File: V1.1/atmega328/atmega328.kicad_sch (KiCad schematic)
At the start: 17 parts

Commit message: things
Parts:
- removed C2, C8, C9: (no value), symbol Device:C_Small
- removed D1: (no value), symbol Device:LED
- removed L1: (no value), symbol Device:L
- removed R6: (no value), symbol Device:R
- removed U2: (no value), symbol Regulator_Switching:TPS62203DBV
- added C2: 4.7, Capacitor_Tantalum_SMD:CP_EIA-3216-18_Kemet-A, symbol Device:C_Polarized_Small
- added C5, C?: 100n, Capacitor_SMD:C_0402_1005Metric, symbol Device:C_Small
- added C6: 20p, Capacitor_SMD:C_0402_1005Metric, symbol Device:C_Small
- added D1: BZV55C6V2, Diode_SMD:D_MiniMELF, symbol Diode:BZV55B10
- added D2: RED_LED, LED_SMD:LED_0603_1608Metric, symbol Device:LED_Small
- added J1: Conn_01x08_Female, Connector_PinSocket_2.54mm:PinSocket_1x08_P2.54mm_Vertical, symbol Connector:Conn_01x08_Female
- added J3: Conn_01x02_Male, Connector_PinHeader_2.54mm:PinHeader_1x02_P2.54mm_Vertical, symbol Connector:Conn_01x02_Male
- added J?: Conn_01x04_Female, Connector_PinSocket_2.54mm:PinSocket_1x04_P2.54mm_Vertical, symbol Connector:Conn_01x04_Female
- added JP1: SolderJumper_2_Open, Jumper:SolderJumper-2_P1.3mm_Open_Pad1.0x1.5mm, symbol Jumper:SolderJumper_2_Open
- added JP? (x3): SolderJumper_3_Open, Jumper:SolderJumper-3_P1.3mm_Open_RoundedPad1.0x1.5mm_NumberLabels, symbol Jumper:SolderJumper_3_Open
- added Q1: Si2319CDS, Package_TO_SOT_SMD:SOT-23, symbol Transistor_FET:Si2319CDS
- added R2: 10k, Resistor_SMD:R_0603_1608Metric, symbol Device:R_Small
- added R3: 20k, Resistor_SMD:R_0603_1608Metric, symbol Device:R_Small
- +5V1: renamed from 3.3v1; value (none) -> Conn_01x01; footprint (none) -> Connector_PinHeader_2.54mm:PinHeader_1x01_P2.54mm_Vertical
- C1: value (none) -> 100n; footprint (none) -> Capacitor_SMD:C_0603_1608Metric; LCSC (none) -> C346191
- C3, C4: value (none) -> 100n; footprint (none) -> Capacitor_SMD:C_0402_1005Metric; LCSC (none) -> C1525
- C7: value (none) -> 20p; footprint (none) -> Capacitor_SMD:C_0402_1005Metric; LCSC (none) -> C880615
- ISP1: value (none) -> Conn_02x03_Top_Bottom; footprint (none) -> Connector_PinSocket_2.54mm:isp_6pin
- R1: value (none) -> 100k; footprint (none) -> Resistor_SMD:R_0603_1608Metric; LCSC (none) -> C14675
- U1: value (none) -> ATmega328P-AU; footprint (none) -> Package_QFP:TQFP-32_7x7mm_P0.8mm
- Y1: value (none) -> Crystal; footprint (none) -> Crystal:Crystal_SMD_5032-2Pin_5.0x3.2mm; LCSC (none) -> C122521
- gave numbers to parts that had none: 1
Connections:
- net GND: now also R1.2, U3.13 (GND), C2.2, C5.2, C6.2, C?.2, J1.7 (Pin_7), J?.1 (Pin_1), JP1.1 (A), R3.1
- net LED_PWR: no longer R1.1
- net MISO: now also U3.3 (MISO)
- net MOSI: now also U3.4 (MOSI)
- net RESET: now also R2.1
- net RX: now also J?.3 (Pin_3)
- net SCK: now also U3.2 (CLK)
- net TX: now also J?.2 (Pin_2)
- net XTAL1: now also C6.1; no longer C3.1
- net XTAL2: now also C7.1; no longer C4.1
- net Wuc: now reaches U1.25 (PC2)
- net Wuc: now also JP?.3 (B)
- net CS: now reaches U3.1 (~{CS})
- net Uas: now reaches U3.10 (U)
- net Uas: now also JP?.1 (A)
- net +5V: now reaches U3.11 (VDD)
- net +5V: now also +5V1.1 (Pin_1), C3.1, C4.1, U1.6 (VCC), C5.1, C?.1, D1.1 (K), D2.2 (A), J?.4 (Pin_4), Q1.2 (S), R2.2
- net Was: now reaches U3.8 (W/PWM)
- net Was: now also JP?.1 (A)
- net Vas: now reaches U3.9 (V)
- net Vas: now also JP?.1 (A)
- removed net +3V3: +5V1.1 (Pin_1), C7.1, ISP1.2 (Pin_2), U1.18 (AVCC), U1.4 (VCC), U1.6 (VCC)
- net LED1 renamed Uuc
- net Uuc: now also JP?.3 (B)
- net LED2 renamed Vuc
- net Vuc: now also JP?.3 (B)
- net VCC renamed Vcc
- net Vcc: now also C2.1, J1.1 (Pin_1), J1.8 (Pin_8), Q1.3 (D)
- new net: D1.2 (A), Q1.1 (G), R1.1
- new net: D2.1 (K), R3.2
- new net 3.3V: ISP1.2 (Pin_2)
- new net DCAP2: U1.4 (VCC)
- new net DCAP3: U1.18 (AVCC)
- new net TRM1: J1.5 (Pin_5), J3.1 (Pin_1)
- new net TRM2: J1.6 (Pin_6), J3.2 (Pin_2), JP1.2 (B)
- new net U: J1.2 (Pin_2), JP?.2 (C)
- new net V: J1.3 (Pin_3), JP?.2 (C)
- new net W: J1.4 (Pin_4), JP?.2 (C)
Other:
- note added: "motor thermistor two wires lead from motor to PCB"
- note added: "reverse polarity protection"
- moved on the sheet: +5V1, ISP1, U1, U3, Y1

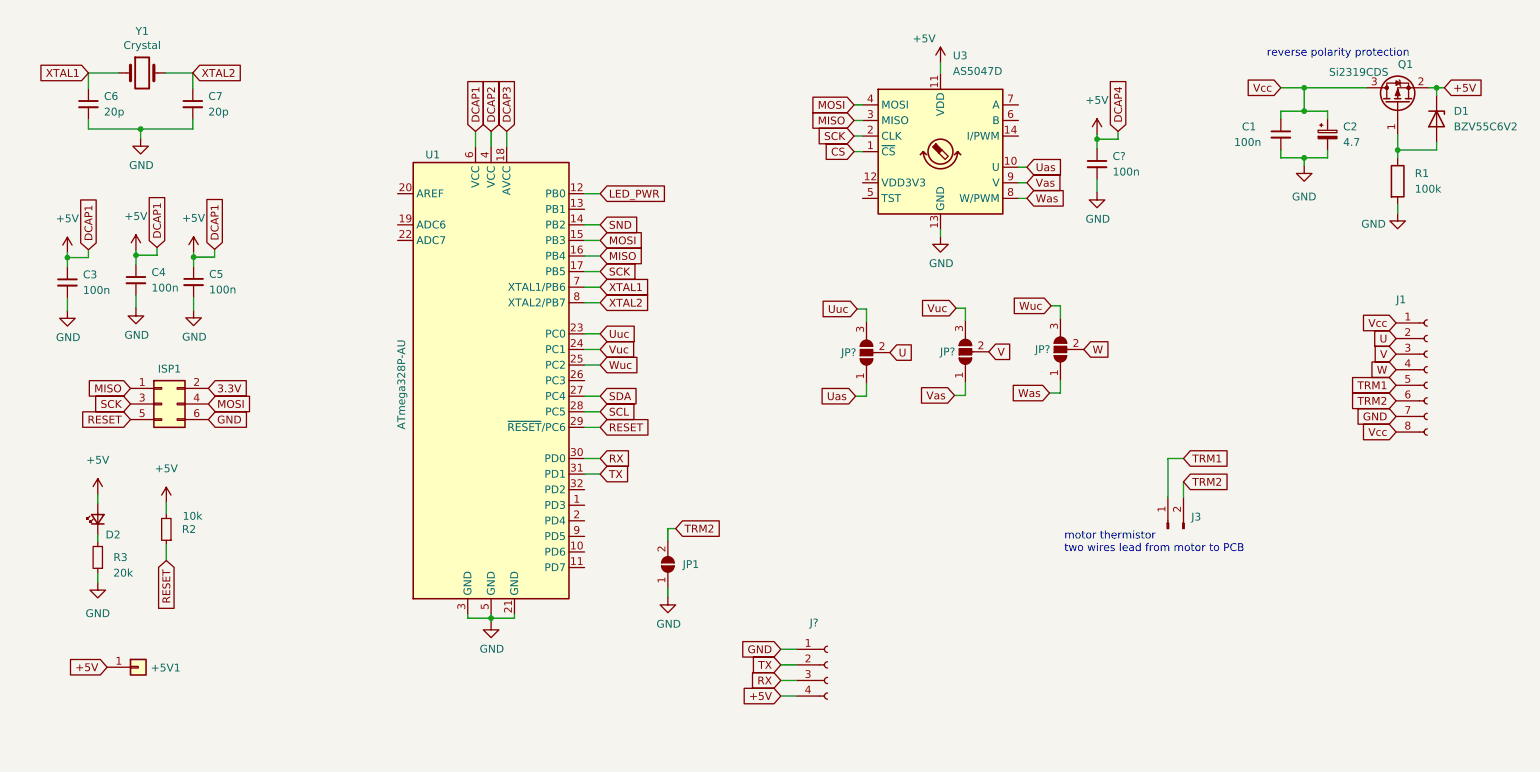
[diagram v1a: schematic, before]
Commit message: recreating lost AS5048 version
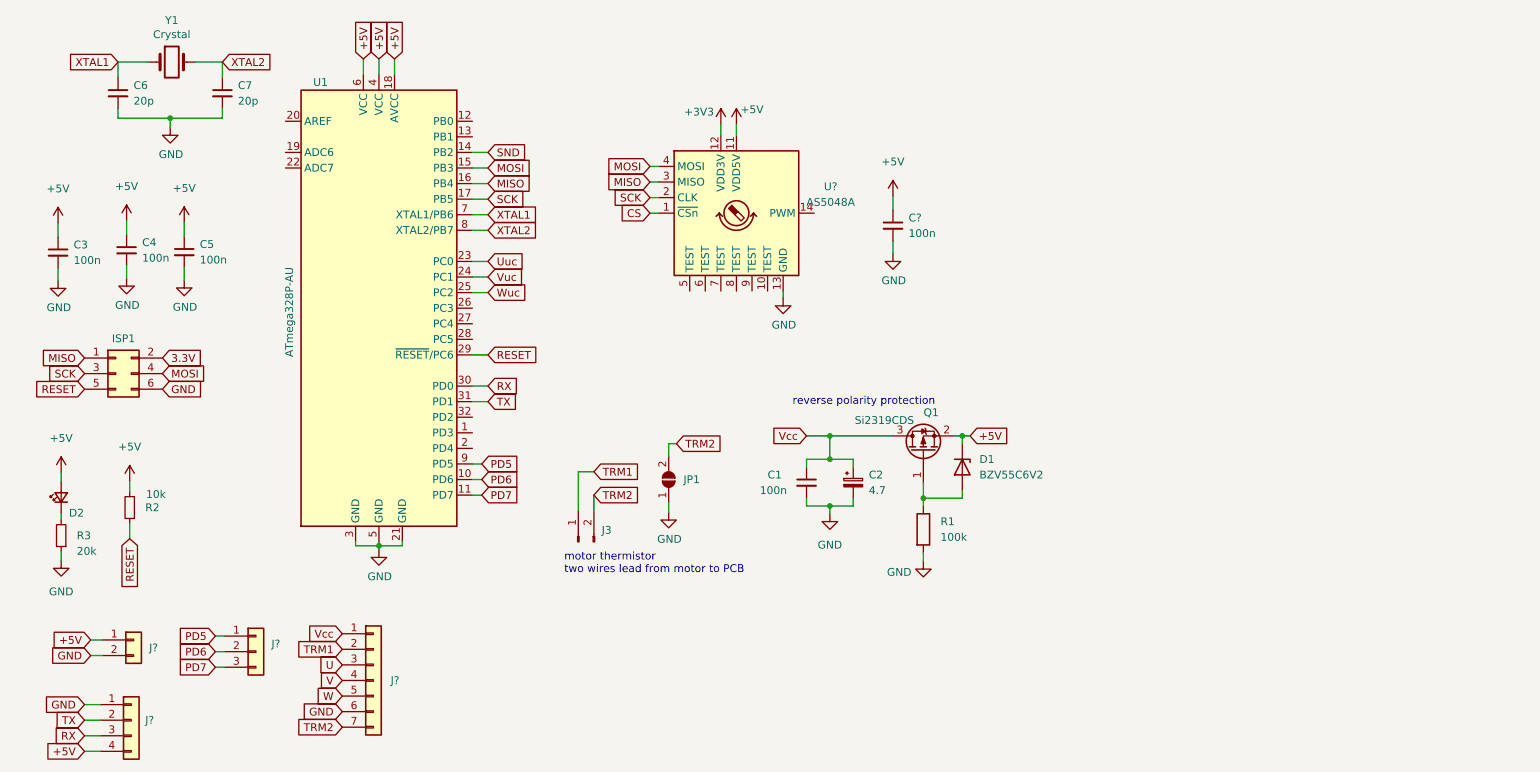
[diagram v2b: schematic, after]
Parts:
- removed +5V1: Conn_01x01, Connector_PinHeader_2.54mm:PinHeader_1x01_P2.54mm_Vertical, symbol Connector_Generic:Conn_01x01
- removed J1: Conn_01x08_Female, Connector_PinSocket_2.54mm:PinSocket_1x08_P2.54mm_Vertical, symbol Connector:Conn_01x08_Female
- removed J?: Conn_01x04_Female, Connector_PinSocket_2.54mm:PinSocket_1x04_P2.54mm_Vertical, symbol Connector:Conn_01x04_Female
- removed JP? (x3): SolderJumper_3_Open, Jumper:SolderJumper-3_P1.3mm_Open_RoundedPad1.0x1.5mm_NumberLabels, symbol Jumper:SolderJumper_3_Open
- removed U3: AS5047D, Package_SO:TSSOP-14_4.4x5mm_P0.65mm, symbol Sensor_Magnetic:AS5047D
- added J?: Conn_01x04, symbol Connector_Generic:Conn_01x04
- added J?: Conn_01x03, symbol Connector_Generic:Conn_01x03
- added J?: Conn_01x07, symbol Connector_Generic:Conn_01x07
- added J?: Conn_01x02, symbol Connector_Generic:Conn_01x02
- added U?: AS5048A, Package_SO:TSSOP-14_4.4x5mm_P0.65mm, symbol Sensor_Magnetic:AS5048A
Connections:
- net DCAP2 is gone; now on net +5V: U1.4 (VCC)
- net DCAP3 is gone; now on net +5V: U1.18 (AVCC)
- net +5V: now also J?.1 (Pin_1), J?.4 (Pin_4), U?.11 (VDD5V)
- net CS: now also U?.1 (~{CSn})
- net GND: now also J?.1 (Pin_1), J?.2 (Pin_2), J?.6 (Pin_6), U?.13 (GND)
- net MISO: now also U?.3 (MISO)
- net MOSI: now also U?.4 (MOSI)
- net RX: now also J?.3 (Pin_3)
- net SCK: now also U?.2 (CLK)
- net TRM1: now also J?.2 (Pin_2)
- net TRM2: now also J?.7 (Pin_7)
- net TX: now also J?.2 (Pin_2)
- net U: now also J?.3 (Pin_3)
- net V: now also J?.4 (Pin_4)
- net Vcc: now also J?.1 (Pin_1)
- net W: now also J?.5 (Pin_5)
- net PD6: now reaches U1.10 (PD6)
- net PD6: now also J?.2 (Pin_2)
- net PD7: now reaches U1.11 (PD7)
- net PD7: now also J?.3 (Pin_3)
- net PD5: now reaches U1.9 (PD5)
- net PD5: now also J?.1 (Pin_1)
- net LED_PWR: no longer names the net of U1.12 (PB0)
- net SCL: no longer names the net of U1.28 (PC5)
- net SDA: no longer names the net of U1.27 (PC4)
- new net +3V3: U?.12 (VDD3V)
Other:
- moved on the sheet: C1, C2, C3, C4, C5, C6, C7, C?, D1, D2, ISP1, J3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

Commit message: recreating lost AS5048 version
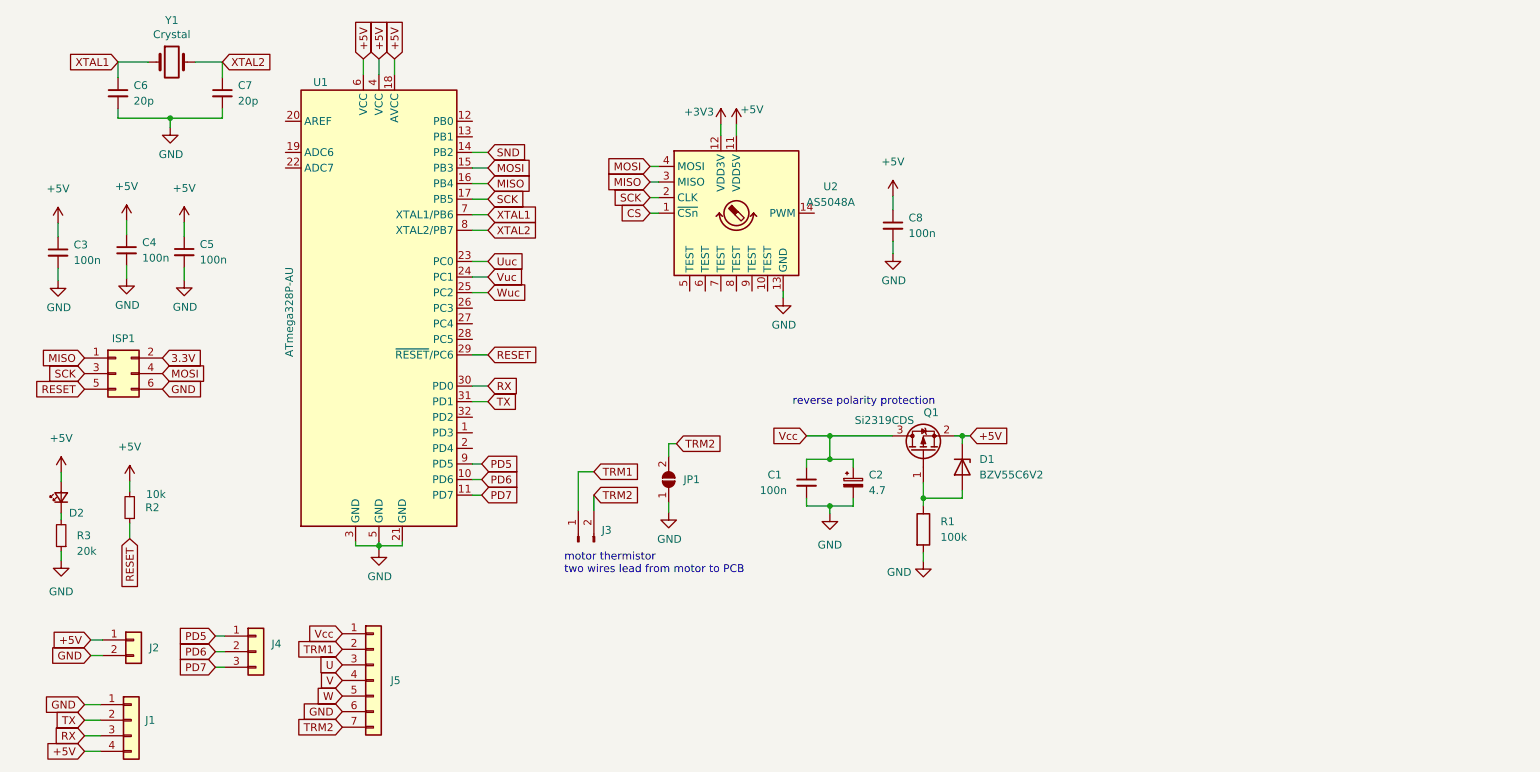
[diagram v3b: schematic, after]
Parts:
- gave numbers to parts that had none: 6
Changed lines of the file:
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@@
   (symbol (lib_id "Connector_Generic:Conn_01x04") (at 34.544 129.794 0) (unit 1)
     (in_bom yes) (on_board yes) (fields_autoplaced)
-    (property "Reference" "J?" (id 0) (at 36.83 129.7939 0)
+    (property "Reference" "J1" (id 0) (at 36.83 129.7939 0)
       (effects (font (size 1.27 1.27)) (justify left))
     )
@@
   (symbol (lib_id "Device:C_Small") (at 158.75 49.149 0) (unit 1)
     (in_bom yes) (on_board yes)
-    (property "Reference" "C?" (id 0) (at 161.29 47.879 0)
+    (property "Reference" "C8" (id 0) (at 161.29 47.879 0)
       (effects (font (size 1.27 1.27)) (justify left))
     )
@@
   (symbol (lib_id "power:GND") (at 140.843 60.96 0) (unit 1)
     (in_bom yes) (on_board yes)
-    (property "Reference" "#PWR?" (id 0) (at 140.843 67.31 0)
+    (property "Reference" "#PWR0102" (id 0) (at 140.843 67.31 0)
       (effects (font (size 1.27 1.27)) hide)
     )
@@
   (symbol (lib_id "power:+3V3") (at 130.683 32.639 0) (unit 1)
     (in_bom yes) (on_board yes)
-    (property "Reference" "#PWR?" (id 0) (at 130.683 36.449 0)
+    (property "Reference" "#PWR0107" (id 0) (at 130.683 36.449 0)
       (effects (font (size 1.27 1.27)) hide)
     )
@@
   (symbol (lib_id "Connector_Generic:Conn_01x03") (at 54.864 118.618 0) (unit 1)
     (in_bom yes) (on_board yes)
-    (property "Reference" "J?" (id 0) (at 57.404 117.3479 0)
+    (property "Reference" "J4" (id 0) (at 57.404 117.3479 0)
       (effects (font (size 1.27 1.27)) (justify left))
     )
@@
   (symbol (lib_id "power:GND") (at 158.75 53.721 0) (unit 1)
     (in_bom yes) (on_board yes)
-    (property "Reference" "#PWR?" (id 0) (at 158.75 60.071 0)
+    (property "Reference" "#PWR0103" (id 0) (at 158.75 60.071 0)
       (effects (font (size 1.27 1.27)) hide)
     )
@@
   (symbol (lib_id "Connector_Generic:Conn_01x07") (at 74.041 123.317 0) (unit 1)
     (in_bom yes) (on_board yes) (fields_autoplaced)
-    (property "Reference" "J?" (id 0) (at 76.835 123.3169 0)
+    (property "Reference" "J5" (id 0) (at 76.835 123.3169 0)
       (effects (font (size 1.27 1.27)) (justify left))
     )
@@
   (symbol (lib_id "power:+5V") (at 158.75 44.323 0) (unit 1)
     (in_bom yes) (on_board yes) (fields_autoplaced)
-    (property "Reference" "#PWR?" (id 0) (at 158.75 48.133 0)
+    (property "Reference" "#PWR0104" (id 0) (at 158.75 48.133 0)
       (effects (font (size 1.27 1.27)) hide)
     )
@@
   (symbol (lib_id "Connector_Generic:Conn_01x02") (at 34.925 116.713 0) (unit 1)
     (in_bom yes) (on_board yes) (fields_autoplaced)
-    (property "Reference" "J?" (id 0) (at 37.465 117.9829 0)
+    (property "Reference" "J2" (id 0) (at 37.465 117.9829 0)
       (effects (font (size 1.27 1.27)) (justify left))
     )
@@
   (symbol (lib_id "power:GND") (at 122.174 95.885 0) (unit 1)
     (in_bom yes) (on_board yes)
-    (property "Reference" "#PWR?" (id 0) (at 122.174 102.235 0)
+    (property "Reference" "#PWR0101" (id 0) (at 122.174 102.235 0)
       (effects (font (size 1.27 1.27)) hide)
     )
@@
   (symbol (lib_id "power:+5V") (at 133.223 32.639 0) (unit 1)
     (in_bom yes) (on_board yes)
-    (property "Reference" "#PWR?" (id 0) (at 133.223 36.449 0)
+    (property "Reference" "#PWR0108" (id 0) (at 133.223 36.449 0)
       (effects (font (size 1.27 1.27)) hide)
     )
@@
   (symbol (lib_id "Sensor_Magnetic:AS5048A") (at 133.223 47.117 0) (unit 1)
     (in_bom yes) (on_board yes) (fields_autoplaced)
-    (property "Reference" "U?" (id 0) (at 148.59 42.7863 0))
+    (property "Reference" "U2" (id 0) (at 148.59 42.7863 0))
     (property "Value" "AS5048A" (id 1) (at 148.59 45.3263 0))
     (property "Footprint" "Package_SO:TSSOP-14_4.4x5mm_P0.65mm" (id 2) (at 133.223 66.167 0)
@@
       (reference "#PWR015") (unit 1) (value "GND") (footprint "")
     )
+    (path "/867f3a2e-72e0-4b88-816f-d18f31d70483"
+      (reference "#PWR0101") (unit 1) (value "GND") (footprint "")
+    )
+    (path "/1a70d9a7-cb73-4892-b131-273ff8ec7a67"
+      (reference "#PWR0102") (unit 1) (value "GND") (footprint "")
+    )
+    (path "/68940270-0d02-41fa-b70d-b2c89618d224"
+      (reference "#PWR0103") (unit 1) (value "GND") (footprint "")
+    )
+    (path "/7a386484-a636-4f6c-bbdf-3059185d06bf"
+      (reference "#PWR0104") (unit 1) (value "+5V") (footprint "")
+    )
     (path "/00000000-0000-0000-0000-000062cb1d4c"
       (reference "#PWR0105") (unit 1) (value "GND") (footprint "")
@@
       (reference "#PWR0106") (unit 1) (value "GND") (footprint "")
     )
-    (path "/1a70d9a7-cb73-4892-b131-273ff8ec7a67"
-      (reference "#PWR?") (unit 1) (value "GND") (footprint "")
-    )
     (path "/37240edb-2cf8-4461-b033-a9a1e16326de"
-      (reference "#PWR?") (unit 1) (value "+3V3") (footprint "")
-    )
-    (path "/68940270-0d02-41fa-b70d-b2c89618d224"
-      (reference "#PWR?") (unit 1) (value "GND") (footprint "")
-    )
-    (path "/7a386484-a636-4f6c-bbdf-3059185d06bf"
-      (reference "#PWR?") (unit 1) (value "+5V") (footprint "")
-    )
-    (path "/867f3a2e-72e0-4b88-816f-d18f31d70483"
-      (reference "#PWR?") (unit 1) (value "GND") (footprint "")
+      (reference "#PWR0107") (unit 1) (value "+3V3") (footprint "")
     )
     (path "/db2fb4f6-7319-4d19-8080-76be12a220c6"
-      (reference "#PWR?") (unit 1) (value "+5V") (footprint "")
+      (reference "#PWR0108") (unit 1) (value "+5V") (footprint "")
     )
     (path "/2c89c050-b532-4895-8f21-83a761d812fb"
@@
     )
     (path "/0e078ae9-8317-4ed9-87d9-5c2f38d357da"
-      (reference "C?") (unit 1) (value "100n") (footprint "Capacitor_SMD:C_0402_1005Metric")
+      (reference "C8") (unit 1) (value "100n") (footprint "Capacitor_SMD:C_0402_1005Metric")
     )
     (path "/9d4896c0-71c0-408c-a483-cfbfb4cd54b4"
@@
       (reference "ISP1") (unit 1) (value "Conn_02x03_Top_Bottom") (footprint "Connector_PinSocket_2.54mm:isp_6pin")
     )
+    (path "/04013dca-8116-4a03-b1b1-6aad3eddb36d"
+      (reference "J1") (unit 1) (value "Conn_01x04") (footprint "")
+    )
+    (path "/7a55b174-5cc7-4525-80d2-2644b42a21b5"
+      (reference "J2") (unit 1) (value "Conn_01x02") (footprint "")
+    )
     (path "/55f70e6c-6342-4715-b8ba-c17f5a663a44"
       (reference "J3") (unit 1) (value "Conn_01x02_Male") (footprint "Connector_PinHeader_2.54mm:PinHeader_1x02_P2.54mm_Vertical")
     )
-    (path "/04013dca-8116-4a03-b1b1-6aad3eddb36d"
-      (reference "J?") (unit 1) (value "Conn_01x04") (footprint "")
-    )
     (path "/56107381-a1b3-4be1-8d54-6548558abaee"
-      (reference "J?") (unit 1) (value "Conn_01x03") (footprint "")
+      (reference "J4") (unit 1) (value "Conn_01x03") (footprint "")
     )
     (path "/745777f8-386e-40f8-91e4-c09e2aa5a715"
-      (reference "J?") (unit 1) (value "Conn_01x07") (footprint "")
-    )
-    (path "/7a55b174-5cc7-4525-80d2-2644b42a21b5"
-      (reference "J?") (unit 1) (value "Conn_01x02") (footprint "")
+      (reference "J5") (unit 1) (value "Conn_01x07") (footprint "")
     )
     (path "/38403b41-e4dd-4954-8433-1dfbff3a0ed0"
@@
     )
     (path "/ec58b41e-a03c-43f9-8c18-2cd7e11a9cb6"
-      (reference "U?") (unit 1) (value "AS5048A") (footprint "Package_SO:TSSOP-14_4.4x5mm_P0.65mm")
+      (reference "U2") (unit 1) (value "AS5048A") (footprint "Package_SO:TSSOP-14_4.4x5mm_P0.65mm")
     )
     (path "/00000000-0000-0000-0000-000062c95262"
